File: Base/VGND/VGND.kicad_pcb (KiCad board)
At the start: 2 copper layers, 30 x 84 mm, 25 parts, among them J1 Conn_01x04_Pin, J2 Conn_01x05_Pin, J3 Barrel_Jack_Switch, J4 AudioJack2_Ground, J5 AudioJack2_Ground, Q1 40V, U1 TLE2426xD, U2 OPA1656

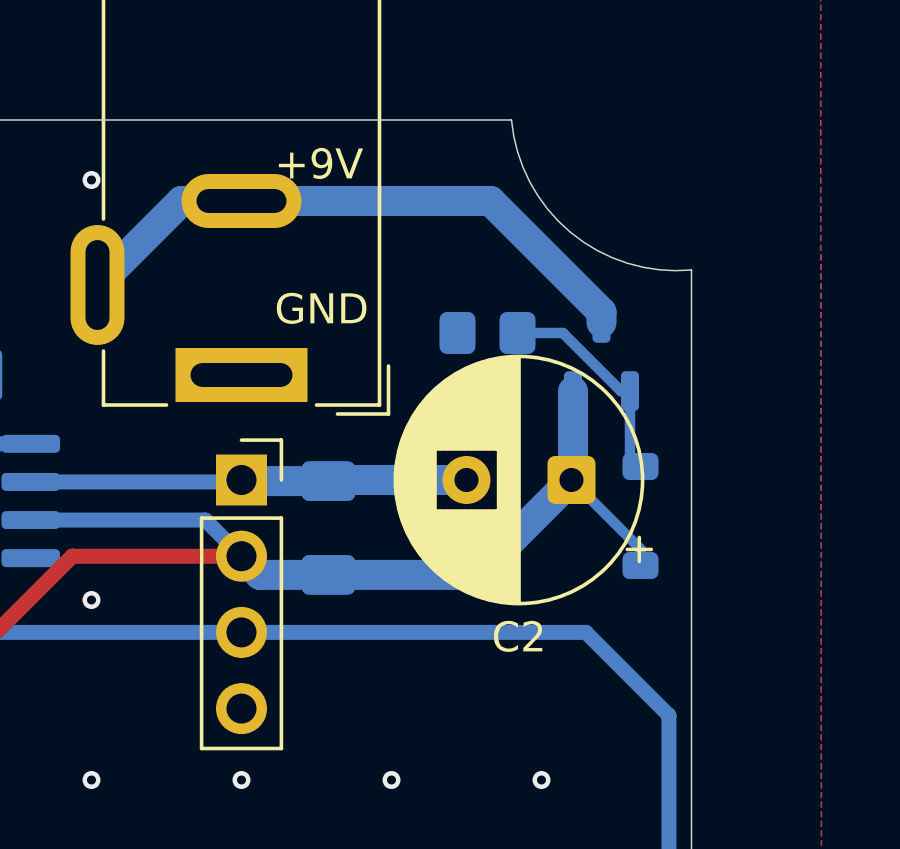
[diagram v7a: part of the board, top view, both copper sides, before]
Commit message: VGND: move THT capacitor up for more room
So the latest round of test builds found a small issue with the base
board: the 100uF THT capacitor needs to lie down on the board, because
the ones I have are too tall at 13mm to stand up straight (11.5mm
between boards).  That was all according to plan.

What was also according to plan was leaving enough space for the extra
audio input or output jack for the joiner/splitter boards.  And that was
a "kind of".  It all worked, but to work well you had to really bend the
capacitor legs so that it moved up on the board before it then lay down
flat on it.

So let's just move the through-holes up a couple of mm so that the
capacitor doesn't need to do some kind of downward dog yoga stretching
thing.

This comes back to the issue that I really should have made a footprint
for the capacitor lying down to make it much more visually obvious,
instead of noticing that things are a bit awkward on the board when
putting it together.

I did know it was a bit tight, and it wasn't really a big problem in
practice.  But it's easy to fix.  Let's be proactive about it so that
next time I build boards I won't have the poor capacitors do
contortions.

The good news? The current boards really do look better noise-wise.  I
noticed it when comparing with one of the previous-gen ones side by side
on the scope while doing the splitter board.  So this really is a fairly
small cosmetic fix.

Signed-off-by: Linus Torvalds <torvalds@linux-foundation.org>
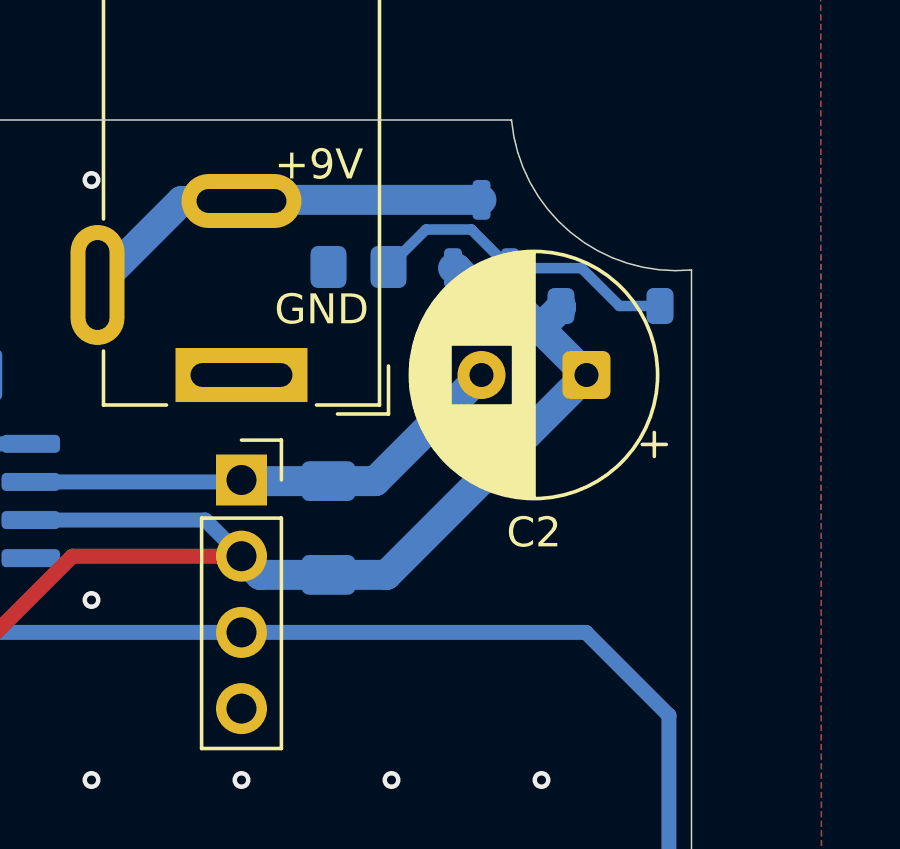
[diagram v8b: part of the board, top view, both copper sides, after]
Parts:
- moved D1 7.07 mm to (112.3, 64.2), turned to 0 degrees
- moved Q1 5.73 mm to (108.0, 61.8)
- moved R1 4.83 mm to (103.9, 62.9)
- moved C2 3.54 mm to (111.5, 66.5)
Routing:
- net PWRIN: track 19.9 -> 14.0 mm
- net Net-(D1-A): track 7.21 -> 10.6 mm
- net VIN: track 115.2 -> 117.4 mm
- net GND: track 14.4 -> 16.4 mm
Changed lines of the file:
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@@
 	(footprint "Capacitor_THT:CP_Radial_D8.0mm_P3.50mm"
 		(layer "F.Cu")
-		(at 111 70 180)
+		(at 111.5 66.5 180)
 		(descr "CP, Radial series, Radial, pin pitch=3.50mm, diameter=8mm, height=12mm, Electrolytic Capacitor")
 		(tags "CP Radial series Radial pin pitch 3.50mm diameter 8mm height 12mm Electrolytic Capacitor")
@@
 	(footprint "Package_TO_SOT_SMD:SOT-23-3"
 		(layer "B.Cu")
-		(at 112 65.9 90)
+		(at 108 61.8 90)
 		(descr "SOT, 3 Pin (JEDEC MO-178 inferred 3-pin variant https://www.jedec.org/document_search?search_api_views_fulltext=MO-178), generated with kicad-footprint-generator ipc_gullwing_generator.py")
 		(tags "SOT TO_SOT_SMD")
@@
 	(footprint "Diode_SMD:D_SOD-123"
 		(layer "B.Cu")
-		(at 113.3 71.2 90)
+		(at 112.3 64.2)
 		(descr "SOD-123")
 		(tags "SOD-123")
 		(property "Reference" "D1"
-			(at 0 0 90)
+			(at 0 0 0)
 			(layer "B.SilkS")
 			(effects
@@
 		)
 		(property "Value" "12V"
-			(at 0 -2.1 90)
+			(at 0 -2.1 0)
 			(layer "B.Fab")
 			(effects
@@
 		)
 		(property "Datasheet" ""
-			(at 0 0 270)
+			(at 0 0 180)
 			(unlocked yes)
 			(layer "B.Fab")
@@
 		)
 		(property "Description" "Zener diode"
-			(at 0 0 270)
+			(at 0 0 180)
 			(unlocked yes)
 			(layer "B.Fab")
@@
 		)
 		(property "Availability" ""
-			(at 0 0 270)
+			(at 0 0 180)
 			(unlocked yes)
 			(layer "B.Fab")
@@
 		)
 		(property "Check_prices" ""
-			(at 0 0 270)
+			(at 0 0 180)
 			(unlocked yes)
 			(layer "B.Fab")
@@
 		)
 		(property "Description_1" ""
-			(at 0 0 270)
+			(at 0 0 180)
 			(unlocked yes)
 			(layer "B.Fab")
@@
 		)
 		(property "MANUFACTURER_PART_NUMBER" ""
-			(at 0 0 270)
+			(at 0 0 180)
 			(unlocked yes)
 			(layer "B.Fab")
@@
 		)
 		(property "MF" ""
-			(at 0 0 270)
+			(at 0 0 180)
 			(unlocked yes)
 			(layer "B.Fab")
@@
 		)
 		(property "MP" ""
-			(at 0 0 270)
+			(at 0 0 180)
 			(unlocked yes)
 			(layer "B.Fab")
@@
 		)
 		(property "PROD_ID" ""
-			(at 0 0 270)
+			(at 0 0 180)
 			(unlocked yes)
 			(layer "B.Fab")
@@
 		)
 		(property "Package" ""
-			(at 0 0 270)
+			(at 0 0 180)
 			(unlocked yes)
 			(layer "B.Fab")
@@
 		)
 		(property "Price" ""
-			(at 0 0 270)
+			(at 0 0 180)
 			(unlocked yes)
 			(layer "B.Fab")
@@
 		)
 		(property "Sim.Device" "D"
-			(at 0 0 270)
+			(at 0 0 180)
 			(unlocked yes)
 			(layer "B.Fab")
@@
 		)
 		(property "Sim.Pins" "1=K 2=A"
-			(at 0 0 270)
+			(at 0 0 180)
 			(unlocked yes)
 			(layer "B.Fab")
@@
 		)
 		(property "SnapEDA_Link" ""
-			(at 0 0 270)
+			(at 0 0 180)
 			(unlocked yes)
 			(layer "B.Fab")
@@
 		)
 		(property "VENDOR" ""
-			(at 0 0 270)
+			(at 0 0 180)
 			(unlocked yes)
 			(layer "B.Fab")
@@
 		)
 		(fp_line
-			(start 2.35 -1.15)
+			(start -2.35 1.15)
 			(end -2.35 -1.15)
 			(stroke
@@
 		)
 		(fp_line
-			(start 2.35 1.15)
-			(end 2.35 -1.15)
+			(start -2.35 1.15)
+			(end 2.35 1.15)
 			(stroke
 				(width 0.05)
@@
 		)
 		(fp_line
-			(start -2.35 1.15)
+			(start 2.35 -1.15)
 			(end -2.35 -1.15)
 			(stroke
@@
 		)
 		(fp_line
-			(start -2.35 1.15)
-			(end 2.35 1.15)
+			(start 2.35 1.15)
+			(end 2.35 -1.15)
 			(stroke
 				(width 0.05)
@@
 		)
 		(fp_line
-			(start 1.4 -0.9)
-			(end -1.4 -0.9)
+			(start -1.4 -0.9)
+			(end -1.4 0.9)
 			(stroke
 				(width 0.1)
@@
 		)
 		(fp_line
-			(start -1.4 -0.9)
-			(end -1.4 0.9)
+			(start -1.4 0.9)
+			(end 1.4 0.9)
 			(stroke
 				(width 0.1)
@@
 		)
 		(fp_line
-			(start 0.25 -0.4)
+			(start -0.75 0)
 			(end -0.35 0)
 			(stroke
@@
 		)
 		(fp_line
-			(start 0.25 0)
-			(end 0.75 0)
+			(start -0.35 0)
+			(end -0.35 -0.55)
 			(stroke
 				(width 0.1)
@@
 		(fp_line
 			(start -0.35 0)
-			(end -0.35 -0.55)
+			(end -0.35 0.55)
 			(stroke
 				(width 0.1)
@@
 		)
 		(fp_line
-			(start -0.35 0)
-			(end -0.35 0.55)
+			(start 0.25 -0.4)
+			(end -0.35 0)
 			(stroke
 				(width 0.1)
@@
 		)
 		(fp_line
-			(start -0.75 0)
-			(end -0.35 0)
+			(start 0.25 0)
+			(end 0.75 0)
 			(stroke
 				(width 0.1)
@@
 		)
 		(fp_line
-			(start 1.4 0.9)
-			(end 1.4 -0.9)
+			(start 1.4 -0.9)
+			(end -1.4 -0.9)
 			(stroke
 				(width 0.1)
@@
 		)
 		(fp_line
-			(start -1.4 0.9)
-			(end 1.4 0.9)
+			(start 1.4 0.9)
+			(end 1.4 -0.9)
 			(stroke
 				(width 0.1)
@@
 		)
 		(fp_text user "${REFERENCE}"
-			(at 0 2 90)
+			(at 0 2 0)
 			(layer "B.Fab")
 			(effects
@@
 		)
 		(pad "1" smd roundrect
-			(at -1.65 0 90)
+			(at -1.65 0)
 			(size 0.9 1.2)
 			(layers "B.Cu" "B.Mask" "B.Paste")
@@
 		)
 		(pad "2" smd roundrect
-			(at 1.65 0 90)
+			(at 1.65 0)
 			(size 0.9 1.2)
 			(layers "B.Cu" "B.Mask" "B.Paste")
@@
 	(footprint "Resistor_SMD:R_0805_2012Metric_Pad1.20x1.40mm_HandSolder"
 		(layer "B.Cu")
-		(at 108.2 65.1 180)
+		(at 103.9 62.9 180)
 		(descr "Resistor SMD 0805 (2012 Metric), square (rectangular) end terminal, IPC-7351 nominal with elongated pad for handsoldering. (Body size source: IPC-SM-782 page 72, https://www.pcb-3d.com/wordpress/wp-content/uploads/ipc-sm-782a_amendment_1_and_2.pdf), generated with kicad-footprint-generator")
 		(tags "resistor handsolder")
@@
 	)
 	(segment
+		(start 107.05 62.9375)
+		(end 107.150558 62.9375)
+		(width 1)
+		(layer "B.Cu")
+		(net 1)
+	)
+	(segment
 		(start 98.2625 114)
 		(end 98.2625 115.9325)
@@
 	)
 	(segment
-		(start 111 70)
-		(end 107.8375 73.1625)
+		(start 109.95 64.95)
+		(end 111.5 66.5)
+		(width 1)
+		(layer "B.Cu")
+		(net 1)
+	)
+	(segment
+		(start 110.65 64.25)
+		(end 109.95 64.95)
 		(width 1)
 		(layer "B.Cu")
@@
 	)
 	(segment
-		(start 107.8375 73.1625)
-		(end 102.9 73.1625)
+		(start 102.9 73.1625)
+		(end 104.8375 73.1625)
 		(width 1)
 		(layer "B.Cu")
@@
 	)
 	(segment
-		(start 111.05 67.0375)
-		(end 111.05 69.95)
+		(start 107.150558 62.9375)
+		(end 108.464058 64.251)
 		(width 1)
 		(layer "B.Cu")
@@
 	)
 	(segment
-		(start 113.3 72.85)
-		(end 113.3 72.3)
-		(width 0.35)
+		(start 110.65 64.2)
+		(end 110.65 64.25)
+		(width 1)
+		(layer "B.Cu")
+		(net 1)
+	)
+	(segment
+		(start 108.464058 64.251)
+		(end 109.251 64.251)
+		(width 1)
 		(layer "B.Cu")
 		(net 1)
@@
 	)
 	(segment
-		(start 113.3 72.3)
-		(end 111 70)
-		(width 0.35)
+		(start 104.8375 73.1625)
+		(end 111.5 66.5)
+		(width 1)
 		(layer "B.Cu")
 		(net 1)
@@
 	)
 	(segment
+		(start 109.251 64.251)
+		(end 109.95 64.95)
+		(width 1)
+		(layer "B.Cu")
+		(net 1)
+	)
+	(segment
 		(start 88.2375 68.5825)
 		(end 88.025 68.795)
@@
 	)
 	(segment
-		(start 107.5 70)
-		(end 102.9375 70)
+		(start 104.4625 70.0375)
+		(end 108 66.5)
+		(width 1)
+		(layer "B.Cu")
+		(net 3)
+	)
+	(segment
+		(start 102.9 70.0375)
+		(end 104.4625 70.0375)
 		(width 1)
 		(layer "B.Cu")
@@
 	)
 	(segment
-		(start 110.712501 65.1)
-		(end 109.2 65.1)
+		(start 112.6 64.2)
+		(end 111.3375 62.9375)
+		(width 0.35)
+		(layer "B.Cu")
+		(net 8)
+	)
+	(segment
+		(start 107.6635 61.651)
+		(end 108.95 62.9375)
 		(width 0.35)
 		(layer "B.Cu")
@@
 	)
 	(segment
-		(start 112.95 69.2)
-		(end 113.3 69.55)
+		(start 113.95 64.2)
+		(end 112.6 64.2)
 		(width 0.35)
 		(layer "B.Cu")
@@
 	)
 	(segment
-		(start 112.95 67.0375)
-		(end 112.95 69.2)
+		(start 106.149 61.651)
+		(end 107.6635 61.651)
 		(width 0.35)
 		(layer "B.Cu")
@@
 	)
 	(segment
-		(start 112.650001 67.0375)
-		(end 110.712501 65.1)
+		(start 111.3375 62.9375)
+		(end 108.95 62.9375)
 		(width 0.35)
 		(layer "B.Cu")
@@
 	)
 	(segment
-		(start 112.95 67.0375)
-		(end 112.650001 67.0375)
+		(start 104.9 62.9)
+		(end 106.149 61.651)
 		(width 0.35)
 		(layer "B.Cu")
@@
 	)
 	(segment
-		(start 108.3 60.7)
-		(end 112 64.4)
+		(start 100.0375 60.6625)
+		(end 100 60.7)
 		(width 1)
 		(layer "B.Cu")
@@
 	(segment
 		(start 100 60.7)
-		(end 108.3 60.7)
-		(width 1)
-		(layer "B.Cu")
-		(net 22)
-	)
-	(segment
-		(start 112 64.4)
-		(end 112 64.7625)
+		(end 98 60.7)
 		(width 1)
 		(layer "B.Cu")
@@
 	)
 	(segment
-		(start 100 60.7)
-		(end 98 60.7)
+		(start 108 60.6625)
+		(end 100.0375 60.6625)
 		(width 1)
 		(layer "B.Cu")
